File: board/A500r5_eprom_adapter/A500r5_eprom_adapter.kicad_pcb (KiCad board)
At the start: 2 copper layers, 10 parts, among them J1 PWR, J2 A18 Selector, J3 A19 Selector, U1 27C400-A500, U2 27C080-L, U3 27C080-L

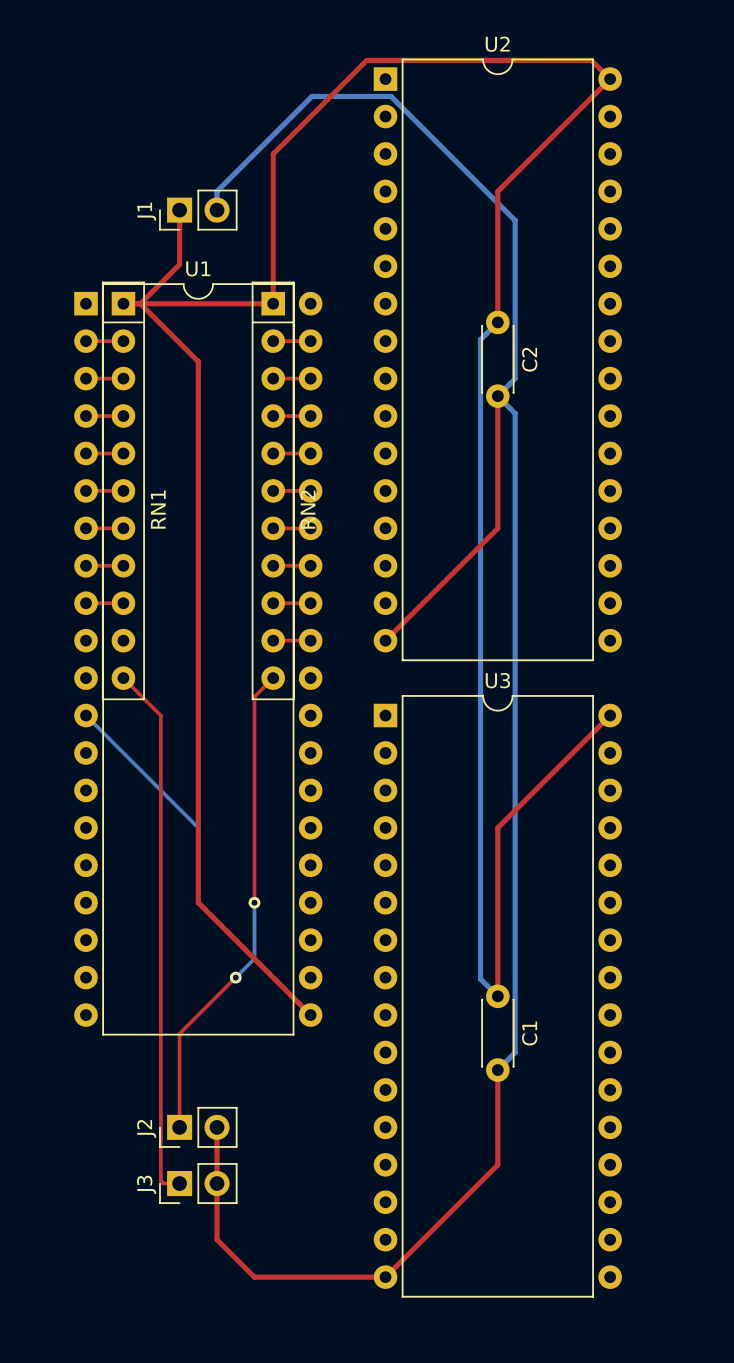
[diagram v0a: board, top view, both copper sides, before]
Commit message: Changed to eeprom adapter
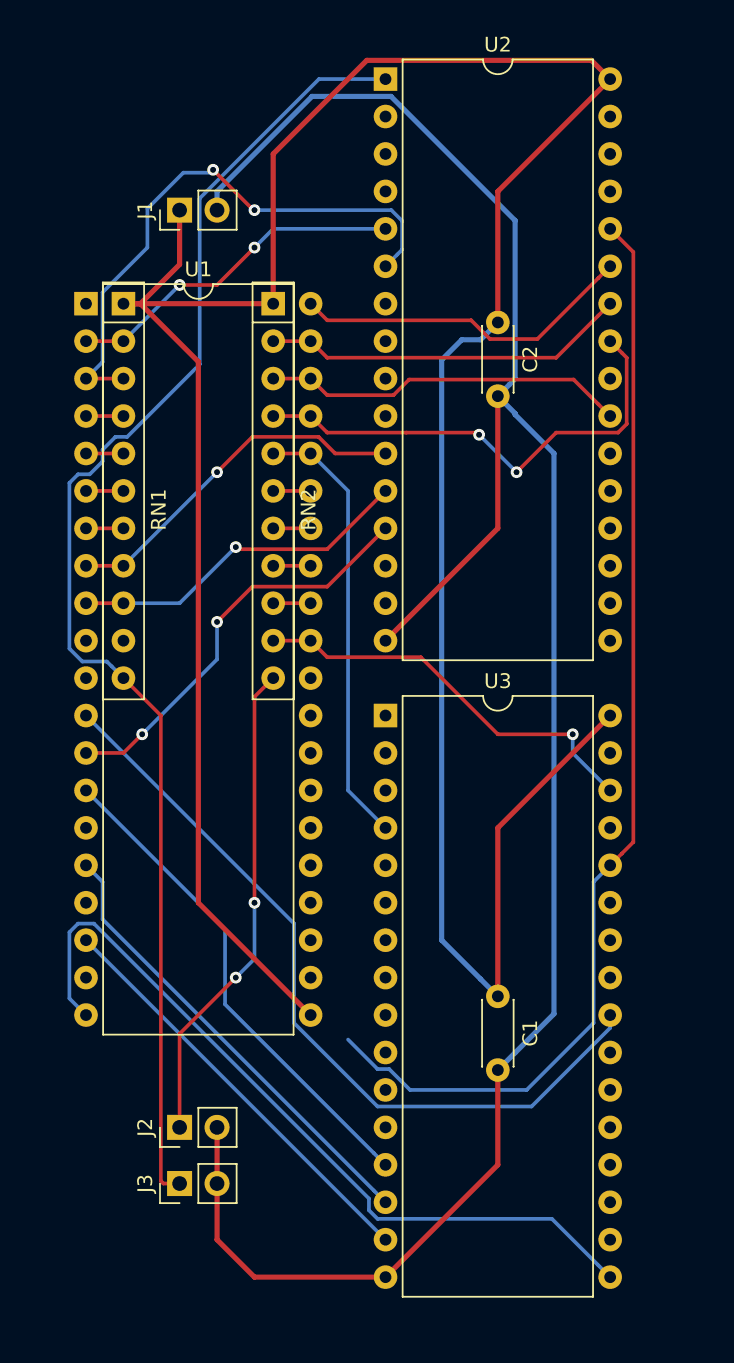
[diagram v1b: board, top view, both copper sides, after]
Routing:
- net /A13: track 2.54 -> 78.1 mm
- net /A19: track 36.5 -> 92.1 mm
- net /D3-H: track 0.00 -> 53.4 mm
- net /~OE: track 10.8 -> 53.6 mm
- net /A6: track 2.54 -> 39.5 mm, vias 0 -> 2
- net /D0-H: track 0.00 -> 33.8 mm
- net /D1-H: track 0.00 -> 31.3 mm
- net /A11: track 2.54 -> 33.0 mm, vias 0 -> 2
- net /D2-H: track 0.00 -> 28.7 mm
- net /D0-L: track 0.00 -> 28.1 mm, vias 0 -> 2
- net /A12: track 2.54 -> 30.0 mm
- net /A17: track 2.54 -> 27.8 mm, vias 0 -> 1
- net /A8: track 0.00 -> 23.4 mm
- net /A9: track 2.54 -> 24.8 mm
- net /A10: track 2.54 -> 24.8 mm
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
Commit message: More changes to the circuit
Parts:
- C1, C2: moved to B.Cu
- moved C1 19.4 mm to (138.4, 99.1), turned to 180 degrees
- moved C2 15.7 mm to (138.4, 57.1), turned to 180 degrees
- moved U2 1.80 mm to (128.3, 57.1)
- moved U3 1.27 mm to (128.3, 99.1)
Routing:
- net /A8: track 23.4 -> 159.9 mm, vias 0 -> 1
- net /A4: track 2.54 -> 101.5 mm, vias 0 -> 1
- net /D3-L: track 0.00 -> 95.0 mm, vias 0 -> 1
- net /A12: track 30.0 -> 110.2 mm, vias 0 -> 2
- net /A3: track 2.54 -> 75.5 mm
- net /A5: track 2.54 -> 74.4 mm
- net /A2: track 2.54 -> 73.6 mm
- net /A16: track 2.54 -> 72.2 mm, vias 0 -> 4
- net /~CE: track 0.00 -> 68.2 mm
- net /A19: track 92.1 -> 158.1 mm, vias 0 -> 1
- net VCC: track 199.5 -> 137.7 mm, vias 0 -> 1
- net GND: track 146.0 -> 202.3 mm, vias 0 -> 2
- net /~OE: track 53.6 -> 0.00 mm
- net /A7: track 23.5 -> 72.1 mm, vias 2 -> 0
- net /A1: track 24.4 -> 72.5 mm, vias 1 -> 0
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
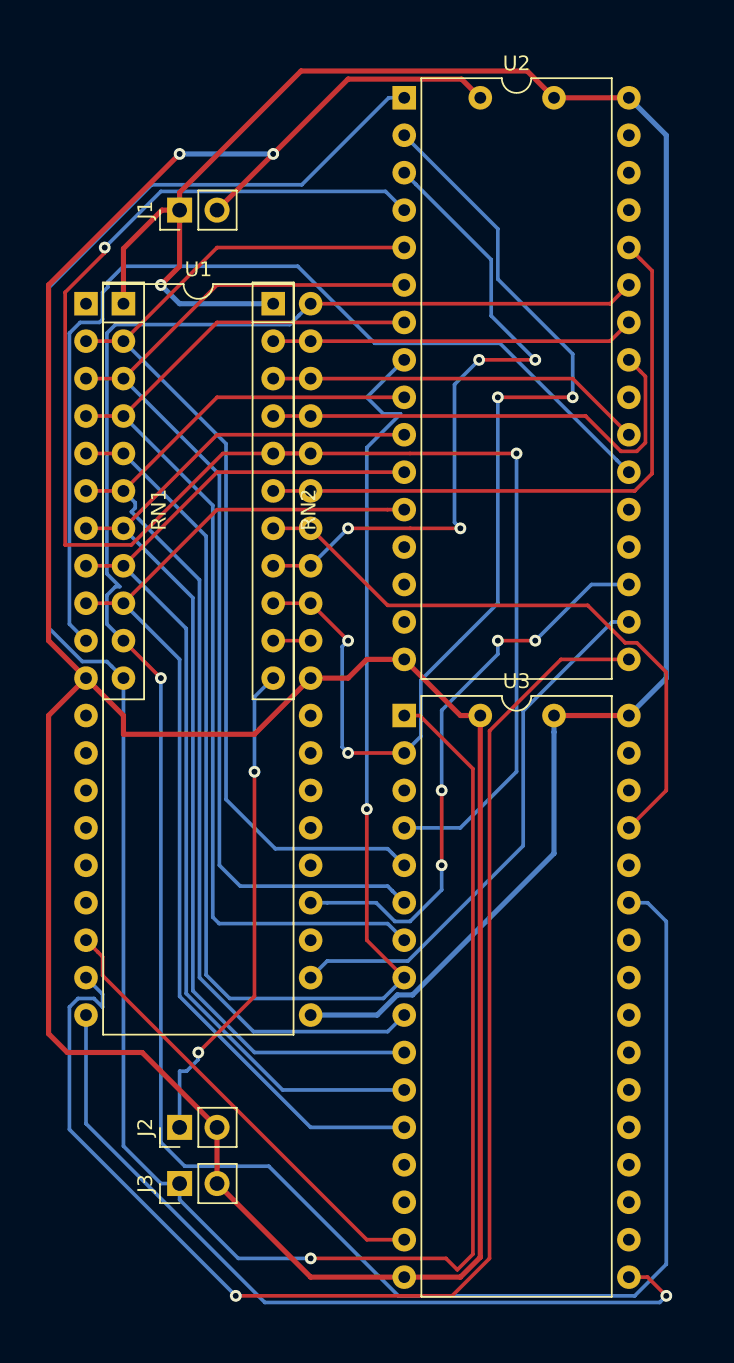
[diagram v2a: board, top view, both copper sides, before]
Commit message: Complete drawing of eprom adapter
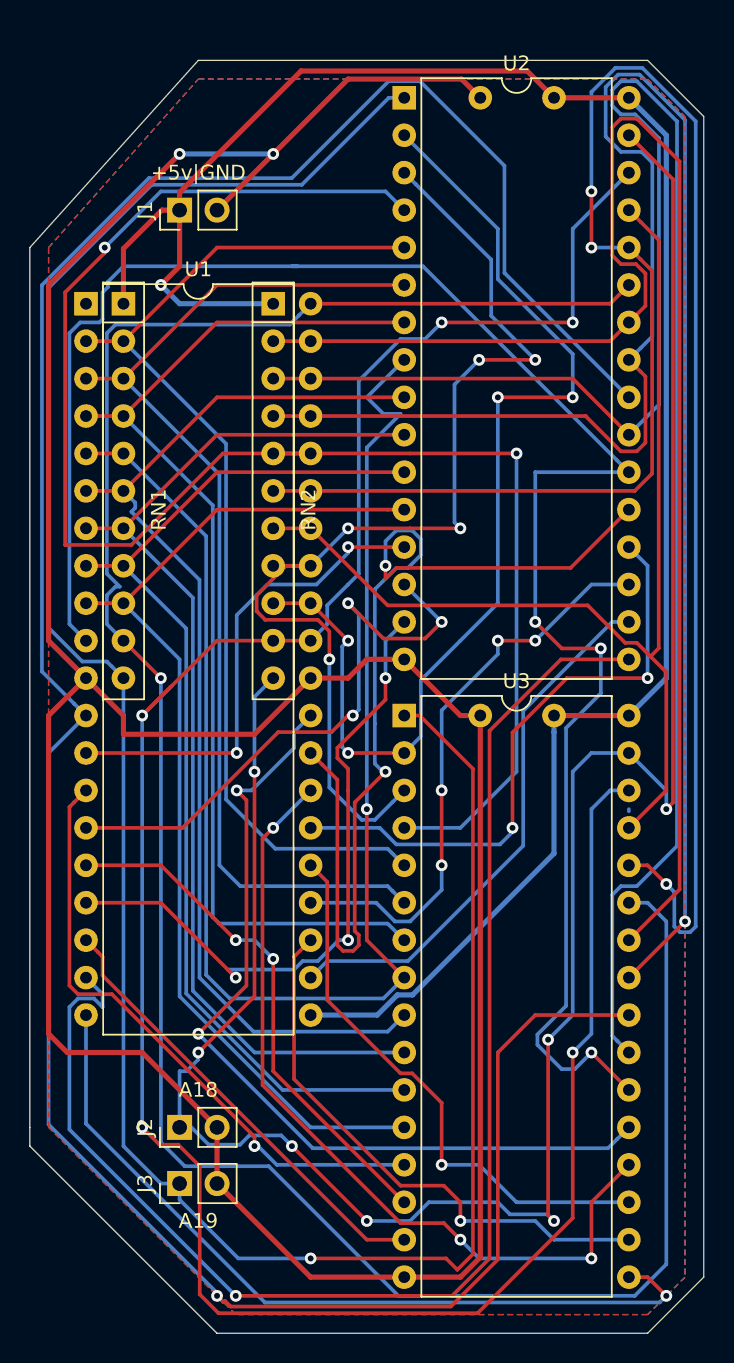
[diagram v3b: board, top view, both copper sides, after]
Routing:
- net /~OE: track 0.00 -> 179.0 mm, vias 0 -> 1
- net /A17: track 2.54 -> 164.7 mm, vias 0 -> 5
- net /A18: track 33.4 -> 151.8 mm, vias 2 -> 7
- net /A10: track 25.7 -> 123.7 mm
- net /A11: track 32.6 -> 120.6 mm, vias 0 -> 1
- net /A13: track 42.2 -> 127.1 mm, vias 0 -> 3
- net /A9: track 24.7 -> 100.2 mm
- net /D7-L: track 0.00 -> 70.2 mm, vias 0 -> 2
- net /~CE: track 68.2 -> 127.4 mm, vias 0 -> 3
- net /D7-H: track 0.00 -> 58.9 mm, vias 0 -> 2
- net /D6-H: track 0.00 -> 55.9 mm, vias 0 -> 3
- net /D2-L: track 0.00 -> 45.8 mm, vias 0 -> 3
- net /D0-H: track 0.00 -> 41.8 mm, vias 0 -> 1
- net /D6-L: track 0.00 -> 41.8 mm, vias 0 -> 2
- net /D1-L: track 0.00 -> 40.7 mm, vias 0 -> 3
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- added copper zone on B.Cu, net GND
- added copper zone on F.Cu, net GND
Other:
- board outline added: 45.7 x 86.4 mm
- board text added: "+5v|GND"
- board text added: "27C040/27C080 HIGH BYTE"
- board text added: "27C040/27C080 LOW BYTE"
- board text added: "A18"
- board text added: "A19"
- board text added: "A500 - 27C0x0 EPROM Adapter"
